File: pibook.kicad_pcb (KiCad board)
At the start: 2 copper layers, 85 x 85 mm, 122 parts, among them IC1 ATTINY48-A, J1 ComputeModule, J2 TRS_JACK_3PIN, P1 CONN_01X40, P2 USB_OTG, P3 CONN_01X02, P4 CONN_02X05, P5 USB_A, P6 CONN_02X06, P7 CONN_01X20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

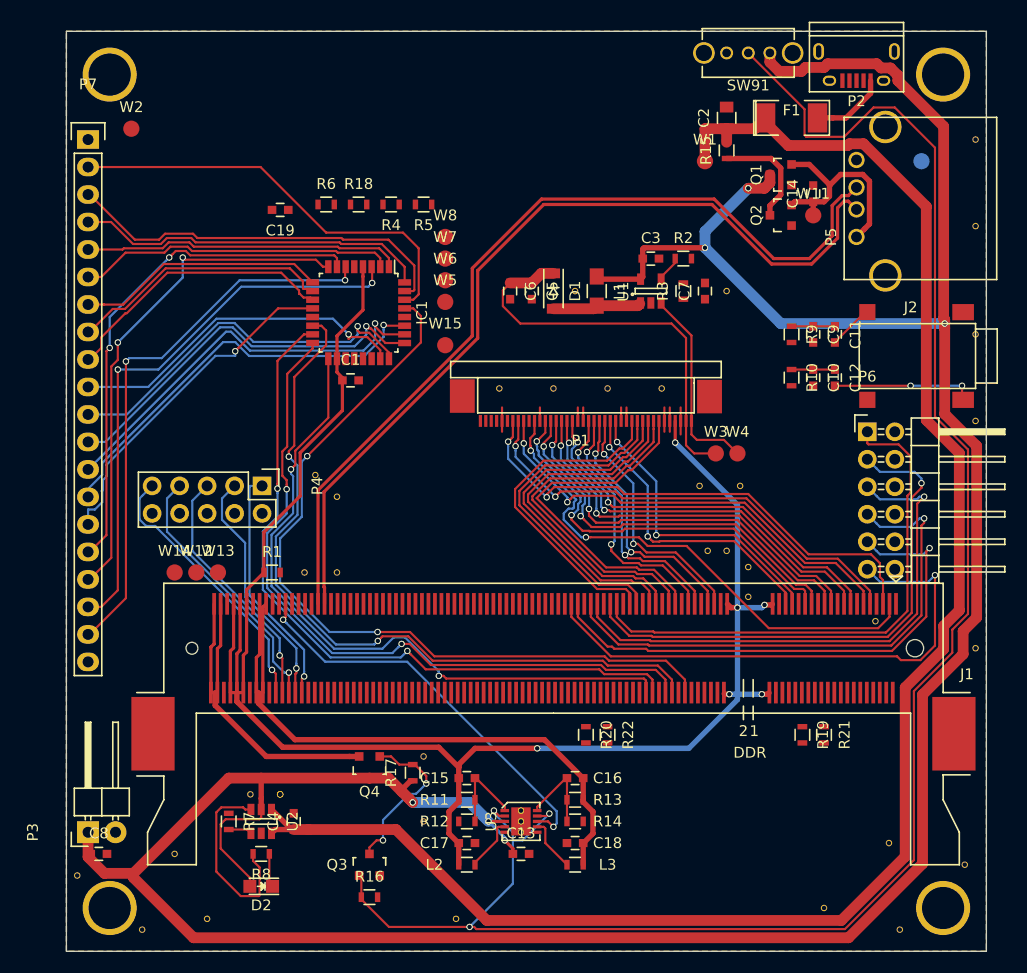
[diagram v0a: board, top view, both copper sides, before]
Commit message: Rounded corners!
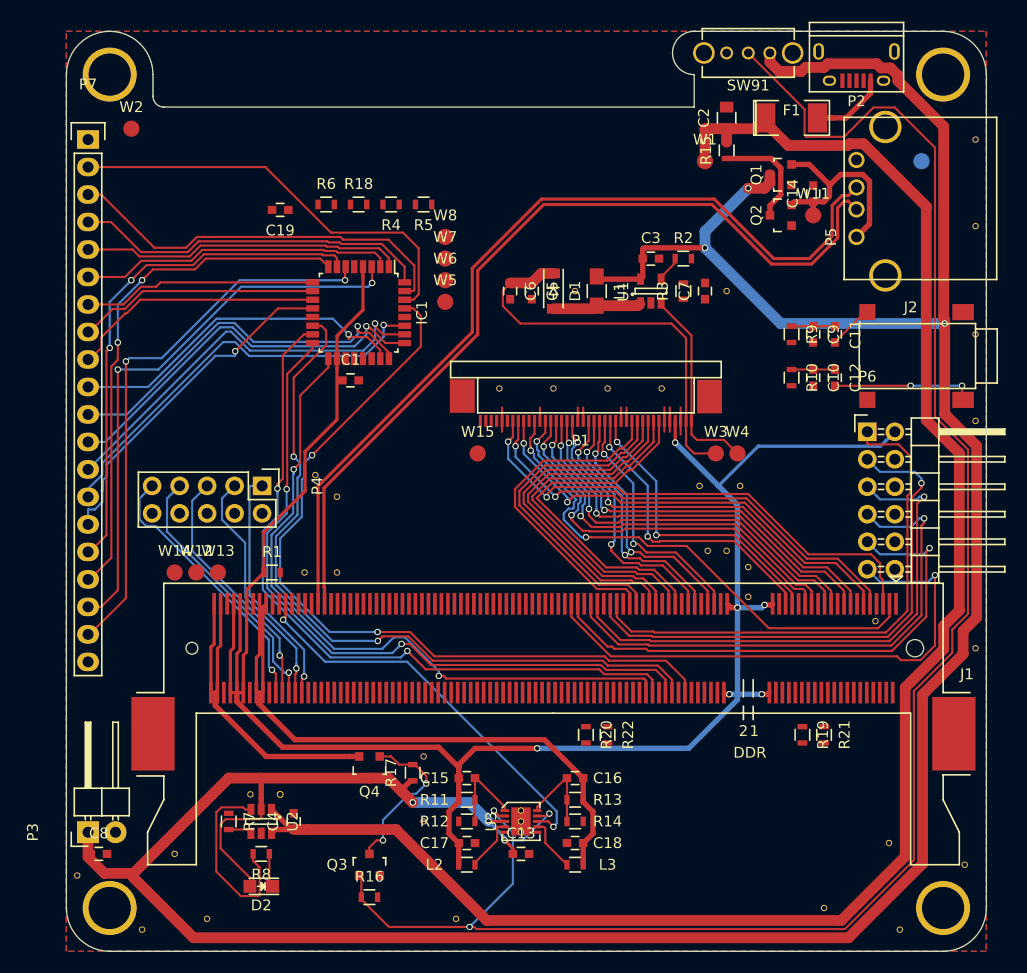
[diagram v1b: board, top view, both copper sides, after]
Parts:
- moved W15 10.4 mm to (111.0, 147.0)
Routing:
- net +3V3: track 161.1 -> 179.0 mm
- net /KEY_C7: track 25.8 -> 23.6 mm
- net /KEY_C6: track 24.4 -> 22.3 mm
- net /KEY_C5: track 23.0 -> 21.6 mm
- net /KEY_R3: track 47.3 -> 48.1 mm
- net /KEY_R2: track 47.2 -> 47.8 mm
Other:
- outline, holes or cut-outs redrawn

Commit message: 5V + some extra routing
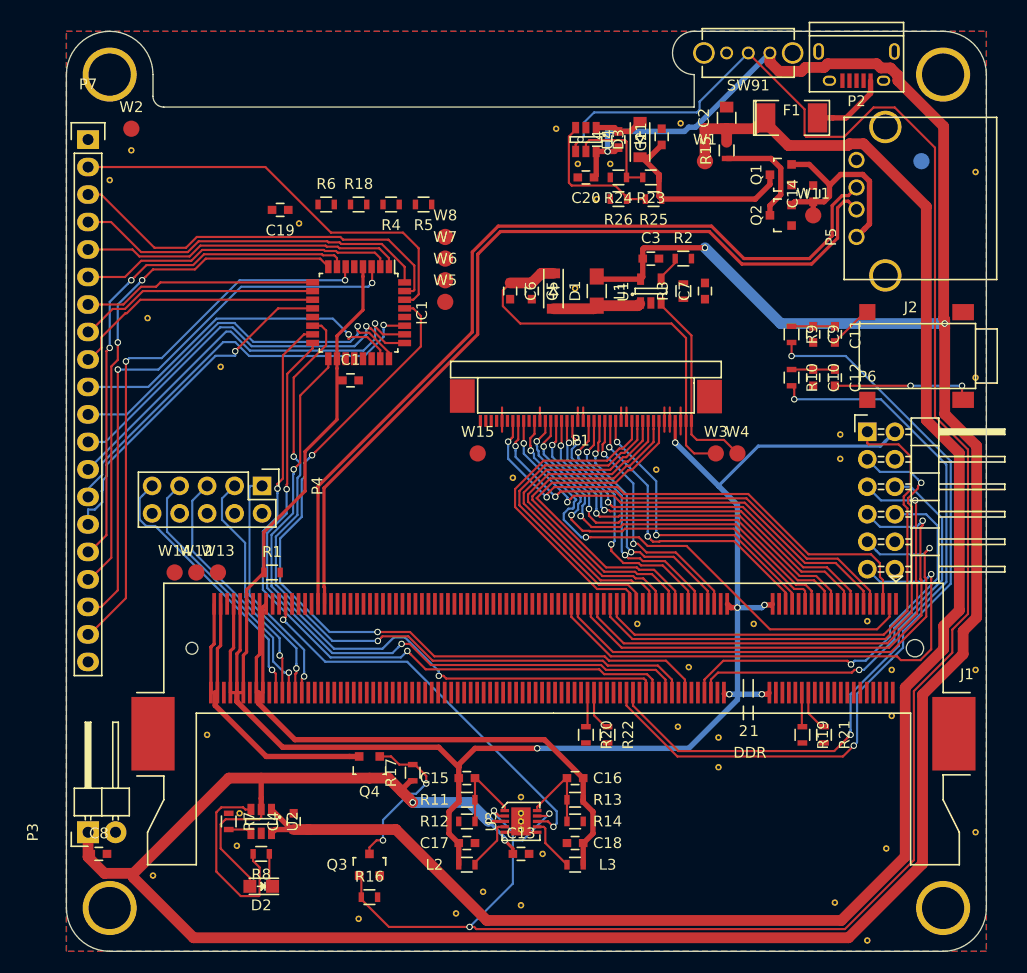
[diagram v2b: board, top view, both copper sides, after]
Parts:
- removed the REF** at (136.0, 157.5)
- removed the REF** at (120.0, 132.0)
- removed the REF** at (136.0, 160.2)
- removed the REF** at (132.2, 156.0)
- removed the REF** at (147.8, 162.5)
- removed the REF** at (96.0, 149.0)
- removed the REF** at (98.0, 151.0)
- removed the REF** at (98.0, 158.0)
- removed the REF** at (95.0, 158.0)
- removed the REF** at (157.0, 118.0)
- removed the REF** at (157.0, 126.0)
- removed the REF** at (134.0, 156.0)
- removed the REF** at (157.0, 136.0)
- removed the REF** at (157.0, 144.0)
- removed the REF** at (157.0, 165.0)
- removed the REF** at (149.0, 183.0)
- removed the REF** at (143.0, 189.0)
- removed the REF** at (86.0, 190.0)
- removed the REF** at (109.0, 190.0)
- removed the REF** at (74.0, 186.0)
- removed the REF** at (80.0, 191.0)
- removed the REF** at (83.0, 184.0)
- removed the REF** at (135.2, 150.0)
- removed the REF** at (90.0, 178.5)
- removed the REF** at (106.0, 181.0)
- removed the REF** at (92.8, 178.5) (x2)
- removed the REF** at (106.0, 175.0)
- removed the REF** at (115.0, 182.0)
- removed the REF** at (115.0, 180.0)
- removed the REF** at (150.0, 191.0)
- removed the REF** at (156.0, 185.0)
- removed the REF** at (131.5, 150.0)
- removed the REF** at (128.0, 141.0)
- removed the REF** at (123.0, 141.0)
- removed the REF** at (118.0, 141.0)
- removed the REF** at (113.0, 141.0)
- removed the REF** at (134.0, 132.0)
- added C20: 1u, Capacitors_SMD:C_0603, F.Cu at (121.0, 121.5)
- added C21: 1u, Capacitors_SMD:C_0603, F.Cu at (128.0, 117.8)
- added D3: MBR0540T3G, Diodes_SMD:SOD-123, F.Cu at (126.0, 118.0)
- added L4: 10u, Capacitors_SMD:C_0603, F.Cu at (124.0, 118.0)
- added R23: 47k, Resistors_SMD:R_0603, F.Cu at (127.0, 121.5)
- added R24: 10k, Resistors_SMD:R_0603, F.Cu at (124.0, 121.5)
- added R25: 40k, Resistors_SMD:R_0603, F.Cu at (127.2, 123.5)
- added R26: 10k, Resistors_SMD:R_0603, F.Cu at (124.0, 123.5)
- added REF**: VIA_0.6MM, ComputeModule:VIA_0.6MM, F.Cu at (144.0, 188.5)
- added REF**: VIA_0.6MM, ComputeModule:VIA_0.6MM, F.Cu at (117.0, 184.0)
- added REF**: VIA_0.6MM, ComputeModule:VIA_0.6MM, F.Cu at (115.0, 181.8)
- added REF**: VIA_0.6MM, ComputeModule:VIA_0.6MM, F.Cu at (115.0, 180.2)
- added REF**: VIA_0.6MM, ComputeModule:VIA_0.6MM, F.Cu at (120.0, 131.8)
- added REF**: VIA_0.6MM, ComputeModule:VIA_0.6MM, F.Cu at (79.0, 119.0)
- added REF**: VIA_0.6MM, ComputeModule:VIA_0.6MM, F.Cu at (94.5, 125.8)
- added REF**: VIA_0.6MM, ComputeModule:VIA_0.6MM, F.Cu at (77.0, 121.8)
- added REF**: VIA_0.6MM, ComputeModule:VIA_0.6MM, F.Cu at (80.5, 134.5)
- added REF**: VIA_0.6MM, ComputeModule:VIA_0.6MM, F.Cu at (87.2, 139.0)
- added REF**: VIA_0.6MM, ComputeModule:VIA_0.6MM, F.Cu at (148.8, 183.5)
- added REF**: VIA_0.6MM, ComputeModule:VIA_0.6MM, F.Cu at (149.2, 167.0)
- added REF**: VIA_0.6MM, ComputeModule:VIA_0.6MM, F.Cu at (130.5, 166.8)
- added REF**: VIA_0.6MM, ComputeModule:VIA_0.6MM, F.Cu at (133.2, 176.0)
- added REF**: VIA_0.6MM, ComputeModule:VIA_0.6MM, F.Cu at (129.5, 172.2)
- added REF**: VIA_0.6MM, ComputeModule:VIA_0.6MM, F.Cu at (115.0, 188.8)
- added REF**: VIA_0.6MM, ComputeModule:VIA_0.6MM, F.Cu at (111.5, 187.5)
- added REF**: VIA_0.6MM, ComputeModule:VIA_0.6MM, F.Cu at (109.0, 189.5)
- added REF**: VIA_0.6MM, ComputeModule:VIA_0.6MM, F.Cu at (88.8, 183.2)
- added REF**: VIA_0.6MM, ComputeModule:VIA_0.6MM, F.Cu at (89.0, 180.2)
- added REF**: VIA_0.6MM, ComputeModule:VIA_0.6MM, F.Cu at (86.0, 173.0)
- added REF**: VIA_0.6MM, ComputeModule:VIA_0.6MM, F.Cu at (149.2, 171.2)
- added REF**: VIA_0.6MM, ComputeModule:VIA_0.6MM, F.Cu at (100.0, 190.0)
- added REF**: VIA_0.6MM, ComputeModule:VIA_0.6MM, F.Cu at (81.0, 186.0)
- added REF**: VIA_0.6MM, ComputeModule:VIA_0.6MM, F.Cu at (157.0, 121.0)
- added REF**: VIA_0.6MM, ComputeModule:VIA_0.6MM, F.Cu at (157.0, 140.0)
- added REF**: VIA_0.6MM, ComputeModule:VIA_0.6MM, F.Cu at (157.0, 167.0)
- added REF**: VIA_0.6MM, ComputeModule:VIA_0.6MM, F.Cu at (157.0, 182.0)
- added REF**: VIA_0.6MM, ComputeModule:VIA_0.6MM, F.Cu at (147.0, 192.0)
- added REF**: VIA_0.6MM, ComputeModule:VIA_0.6MM, F.Cu at (147.0, 162.5)
- added REF**: VIA_0.6MM, ComputeModule:VIA_0.6MM, F.Cu at (136.5, 162.8)
- added REF**: VIA_0.6MM, ComputeModule:VIA_0.6MM, F.Cu at (125.8, 162.8)
- added REF**: VIA_0.6MM, ComputeModule:VIA_0.6MM, F.Cu at (133.2, 173.2)
- added REF**: VIA_0.6MM, ComputeModule:VIA_0.6MM, F.Cu at (129.8, 116.5)
- added REF**: VIA_0.6MM, ComputeModule:VIA_0.6MM, F.Cu at (118.2, 117.0)
- added REF**: VIA_0.6MM, ComputeModule:VIA_0.6MM, F.Cu at (122.0, 123.5)
- added REF**: VIA_0.6MM, ComputeModule:VIA_0.6MM, F.Cu at (123.2, 120.2)
- added REF**: VIA_0.6MM, ComputeModule:VIA_0.6MM, F.Cu at (120.2, 120.2)
- added REF**: VIA_0.6MM, ComputeModule:VIA_0.6MM, F.Cu at (114.2, 149.2)
- added REF**: VIA_0.6MM, ComputeModule:VIA_0.6MM, F.Cu at (127.5, 148.5)
- added REF**: VIA_0.6MM, ComputeModule:VIA_0.6MM, F.Cu at (144.5, 147.5)
- added REF**: VIA_0.6MM, ComputeModule:VIA_0.6MM, F.Cu at (144.5, 145.2)
- added REF**: VIA_0.6MM, ComputeModule:VIA_0.6MM, F.Cu at (115.0, 178.8)
- added U4: MIC2619YD6, TO_SOT_Packages_SMD:SOT-23-6, F.Cu at (121.0, 118.0)
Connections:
- Q1 pad 3: +BATT -> +5V
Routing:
- net /AUDIO_R_PWM: track 0.00 -> 74.5 mm, vias 0 -> 2
- net /AUDIO_L_PWM: track 0.00 -> 70.2 mm, vias 0 -> 2
- net /UART_TX: track 0.00 -> 38.3 mm, vias 0 -> 1
- net /UART_RX: track 0.00 -> 36.7 mm, vias 0 -> 1
- net /PWR_ENABLE: track 170.8 -> 192.0 mm, vias 3 -> 4
- net +5V: track 0.00 -> 18.7 mm
- net +BATT: track 284.8 -> 299.2 mm
- net Net-(R25-Pad2): track 0.00 -> 13.2 mm
- net Net-(R23-Pad2): track 0.00 -> 9.48 mm
- net Net-(D3-Pad2): track 0.00 -> 4.56 mm
- net Net-(J1-Pad28): track 0.00 -> 3.87 mm
- net Net-(J1-Pad82): track 0.00 -> 3.78 mm
- net Net-(J1-Pad84): track 0.00 -> 3.21 mm
- net GND: track 15.5 -> 18.7 mm
- net Net-(J1-Pad30): track 0.00 -> 3.17 mm
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
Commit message: All signals routed (still fails DRC)
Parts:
- added REF**: VIA_0.6MM, ComputeModule:VIA_0.6MM, F.Cu at (152.5, 148.0)
- added REF**: VIA_0.6MM, ComputeModule:VIA_0.6MM, F.Cu at (80.0, 158.8)
- added REF**: VIA_0.6MM, ComputeModule:VIA_0.6MM, F.Cu at (83.2, 164.0)
- added REF**: VIA_0.6MM, ComputeModule:VIA_0.6MM, F.Cu at (83.5, 147.8)
- added REF**: VIA_0.6MM, ComputeModule:VIA_0.6MM, F.Cu at (93.8, 171.0)
- added REF**: VIA_0.6MM, ComputeModule:VIA_0.6MM, F.Cu at (125.0, 172.8)
- added REF**: VIA_0.6MM, ComputeModule:VIA_0.6MM, F.Cu at (99.2, 142.0)
- added REF**: VIA_0.6MM, ComputeModule:VIA_0.6MM, F.Cu at (99.0, 137.0)
- added REF**: VIA_0.6MM, ComputeModule:VIA_0.6MM, F.Cu at (98.2, 133.0)
- moved R18 28.2 mm to (111.0, 150.0)
- moved W8 24.8 mm to (91.0, 145.0), turned to 90 degrees
- moved C19 23.5 mm to (116.0, 121.0), turned to 0 degrees
- moved W7 22.0 mm to (91.0, 143.0), turned to 90 degrees
- moved W6 19.7 mm to (91.0, 141.0), turned to 90 degrees
- moved W5 18.0 mm to (91.0, 139.0), turned to 90 degrees
- moved R4 14.8 mm to (116.0, 117.0)
- moved R6 12.2 mm to (107.0, 131.0), turned to 270 degrees
- moved R5 11.2 mm to (116.0, 119.0), turned to 0 degrees
- moved W13 7.28 mm to (94.0, 156.0)
- moved W12 4.12 mm to (89.0, 157.0)
- moved W14 3.16 mm to (86.0, 157.0)
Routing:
- net /ANALOG1: track 0.00 -> 133.3 mm, vias 0 -> 1
- net /ANALOG0: track 0.00 -> 132.2 mm, vias 0 -> 1
- net /BACKL_PWM: track 2.44 -> 120.0 mm, vias 0 -> 2
- net /LCD_DISP_ON: track 0.00 -> 73.7 mm, vias 0 -> 2
- net +3V3: track 179.0 -> 227.7 mm, vias 6 -> 8
- net Net-(C19-Pad1): track 0.00 -> 27.2 mm, vias 0 -> 2
- net /AVR_~RST: track 74.1 -> 84.5 mm, vias 2 -> 3
- net +1V8: track 59.9 -> 68.8 mm
- net +BATT: track 299.2 -> 306.4 mm, vias 6 -> 7
- net Net-(C12-Pad2): track 13.1 -> 19.9 mm
- net /AVR_SCK: track 63.6 -> 69.1 mm, vias 2 -> 4
- net /AVR_MISO: track 66.6 -> 71.1 mm, vias 2 -> 4
- net /CM_VBAT: track 33.7 -> 37.9 mm
- net GND: track 18.7 -> 22.2 mm
- net /AVR_MOSI: track 67.1 -> 70.5 mm
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
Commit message: Corrected some DRC
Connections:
- J1 pad 10: (no net) -> Net-(J1-Pad10)
- J1 pad 100: (no net) -> Net-(J1-Pad100)
- J1 pad 101: (no net) -> Net-(J1-Pad101)
- J1 pad 102: (no net) -> Net-(J1-Pad102)
- J1 pad 105: (no net) -> Net-(J1-Pad105)
- J1 pad 106: (no net) -> Net-(J1-Pad106)
- J1 pad 107: (no net) -> Net-(J1-Pad107)
- J1 pad 108: (no net) -> Net-(J1-Pad108)
- J1 pad 111: (no net) -> Net-(J1-Pad111)
- J1 pad 112: (no net) -> Net-(J1-Pad112)
- J1 pad 113: (no net) -> Net-(J1-Pad113)
- J1 pad 114: (no net) -> Net-(J1-Pad114)
- J1 pad 117: (no net) -> Net-(J1-Pad117)
- J1 pad 118: (no net) -> Net-(J1-Pad118)
- J1 pad 119: (no net) -> Net-(J1-Pad119)
- J1 pad 12: (no net) -> Net-(J1-Pad12)
- J1 pad 120: (no net) -> Net-(J1-Pad120)
- J1 pad 123: (no net) -> Net-(J1-Pad123)
- J1 pad 124: (no net) -> Net-(J1-Pad124)
- J1 pad 125: (no net) -> Net-(J1-Pad125)
- J1 pad 126: (no net) -> Net-(J1-Pad126)
- J1 pad 128: (no net) -> Net-(J1-Pad128)
- J1 pad 129: (no net) -> Net-(J1-Pad129)
- J1 pad 130: (no net) -> Net-(J1-Pad130)
- J1 pad 131: (no net) -> Net-(J1-Pad131)
- J1 pad 132: (no net) -> Net-(J1-Pad132)
- J1 pad 135: (no net) -> Net-(J1-Pad135)
- J1 pad 136: (no net) -> Net-(J1-Pad136)
- J1 pad 137: (no net) -> Net-(J1-Pad137)
- J1 pad 138: (no net) -> Net-(J1-Pad138)
- J1 pad 14: (no net) -> Net-(J1-Pad14)
- J1 pad 141: (no net) -> Net-(J1-Pad141)
- J1 pad 142: (no net) -> Net-(J1-Pad142)
- J1 pad 143: (no net) -> Net-(J1-Pad143)
- J1 pad 144: (no net) -> Net-(J1-Pad144)
- J1 pad 147: (no net) -> Net-(J1-Pad147)
- J1 pad 148: (no net) -> Net-(J1-Pad148)
- J1 pad 149: (no net) -> Net-(J1-Pad149)
- J1 pad 150: (no net) -> Net-(J1-Pad150)
- J1 pad 153: (no net) -> Net-(J1-Pad153)
- J1 pad 154: (no net) -> Net-(J1-Pad154)
- J1 pad 155: (no net) -> Net-(J1-Pad155)
- J1 pad 156: (no net) -> Net-(J1-Pad156)
- J1 pad 158: (no net) -> Net-(J1-Pad158)
- J1 pad 159: (no net) -> Net-(J1-Pad159)
- J1 pad 16: (no net) -> Net-(J1-Pad16)
- J1 pad 160: (no net) -> Net-(J1-Pad160)
- J1 pad 161: (no net) -> Net-(J1-Pad161)
- J1 pad 162: (no net) -> Net-(J1-Pad162)
- J1 pad 166: (no net) -> Net-(J1-Pad166)
- J1 pad 171: (no net) -> Net-(J1-Pad171)
- J1 pad 173: (no net) -> Net-(J1-Pad173)
- J1 pad 175: (no net) -> Net-(J1-Pad175)
- J1 pad 179: (no net) -> Net-(J1-Pad179)
- J1 pad 18: (no net) -> Net-(J1-Pad18)
- J1 pad 20: (no net) -> Net-(J1-Pad20)
- J1 pad 22: (no net) -> Net-(J1-Pad22)
- J1 pad 24: (no net) -> Net-(J1-Pad24)
- J1 pad 34: (no net) -> Net-(J1-Pad34)
- J1 pad 36: (no net) -> Net-(J1-Pad36)
- J1 pad 4: (no net) -> Net-(J1-Pad4)
- J1 pad 52: (no net) -> Net-(J1-Pad52)
- J1 pad 6: (no net) -> Net-(J1-Pad6)
- J1 pad 76: (no net) -> Net-(J1-Pad76)
- J1 pad 78: (no net) -> Net-(J1-Pad78)
- J1 pad 8: (no net) -> Net-(J1-Pad8)
- J1 pad 88: (no net) -> Net-(J1-Pad88)
- J1 pad 90: (no net) -> Net-(J1-Pad90)
- J1 pad 93: (no net) -> Net-(J1-Pad93)
- J1 pad 94: (no net) -> Net-(J1-Pad94)
- J1 pad 95: (no net) -> Net-(J1-Pad95)
- J1 pad 96: (no net) -> Net-(J1-Pad96)
- J1 pad 99: (no net) -> Net-(J1-Pad99)
- P1 pad 35: (no net) -> Net-(P1-Pad35)
- P1 pad 37: (no net) -> Net-(P1-Pad37)
- P1 pad 38: (no net) -> Net-(P1-Pad38)
- P1 pad 39: (no net) -> Net-(P1-Pad39)
- P1 pad 40: (no net) -> Net-(P1-Pad40)
- P2 pad 2: (no net) -> Net-(P2-Pad2)
- P2 pad 3: (no net) -> Net-(P2-Pad3)
- P2 pad 4: (no net) -> Net-(P2-Pad4)
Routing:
- net /LCD_B_7: track 40.3 -> 37.2 mm
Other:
- net class Default: clearance 0.2 -> 0.199
- rule pad_to_mask_clearance: 0 -> 0.01
- rule trace_clearance: 0.2 -> 0.199

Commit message: Working on new switchmode layout
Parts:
- added TP1: Tie_point, ComputeModule:tiepoint-0.3, F.Cu at (114.5, 182.5)
- moved R14 11.3 mm to (131.0, 183.5)
- moved R13 8.06 mm to (127.0, 183.0)
- moved C15 7.83 mm to (106.5, 184.0)
- moved C16 6.96 mm to (126.5, 179.5)
- moved C18 6.52 mm to (116.5, 177.5)
- moved C13 6.02 mm to (110.5, 180.0), turned to 90 degrees
- moved C17 5.52 mm to (109.5, 177.5)
- moved L3 5.34 mm to (119.0, 179.8), turned to 90 degrees
- moved L2 5.22 mm to (108.5, 180.0), turned to 90 degrees
- moved R12 5.06 mm to (109.2, 186.0)
- moved R11 4.92 mm to (105.5, 181.0)
- moved REF** 4.78 mm to (111.5, 175.5)
- moved REF** 4.37 mm to (104.8, 188.5)
- moved R17 1.25 mm to (104.0, 175.8)
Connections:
- C13 pad 2: GND -> GNDPWR
- C17 pad 2: GND -> GNDPWR
- C18 pad 2: GND -> GNDPWR
- J1 pad 10: Net-(J1-Pad10) -> (no net)
- J1 pad 100: Net-(J1-Pad100) -> (no net)
- J1 pad 101: Net-(J1-Pad101) -> (no net)
- J1 pad 102: Net-(J1-Pad102) -> (no net)
- J1 pad 105: Net-(J1-Pad105) -> (no net)
- J1 pad 106: Net-(J1-Pad106) -> (no net)
- J1 pad 107: Net-(J1-Pad107) -> (no net)
- J1 pad 108: Net-(J1-Pad108) -> (no net)
- J1 pad 111: Net-(J1-Pad111) -> (no net)
- J1 pad 112: Net-(J1-Pad112) -> (no net)
- J1 pad 113: Net-(J1-Pad113) -> (no net)
- J1 pad 114: Net-(J1-Pad114) -> (no net)
- J1 pad 117: Net-(J1-Pad117) -> (no net)
- J1 pad 118: Net-(J1-Pad118) -> (no net)
- J1 pad 119: Net-(J1-Pad119) -> (no net)
- J1 pad 12: Net-(J1-Pad12) -> (no net)
- J1 pad 120: Net-(J1-Pad120) -> (no net)
- J1 pad 123: Net-(J1-Pad123) -> (no net)
- J1 pad 124: Net-(J1-Pad124) -> (no net)
- J1 pad 125: Net-(J1-Pad125) -> (no net)
- J1 pad 126: Net-(J1-Pad126) -> (no net)
- J1 pad 128: Net-(J1-Pad128) -> (no net)
- J1 pad 129: Net-(J1-Pad129) -> (no net)
- J1 pad 130: Net-(J1-Pad130) -> (no net)
- J1 pad 131: Net-(J1-Pad131) -> (no net)
- J1 pad 132: Net-(J1-Pad132) -> (no net)
- J1 pad 135: Net-(J1-Pad135) -> (no net)
- J1 pad 136: Net-(J1-Pad136) -> (no net)
- J1 pad 137: Net-(J1-Pad137) -> (no net)
- J1 pad 138: Net-(J1-Pad138) -> (no net)
- J1 pad 14: Net-(J1-Pad14) -> (no net)
- J1 pad 141: Net-(J1-Pad141) -> (no net)
- J1 pad 142: Net-(J1-Pad142) -> (no net)
- J1 pad 143: Net-(J1-Pad143) -> (no net)
- J1 pad 144: Net-(J1-Pad144) -> (no net)
- J1 pad 147: Net-(J1-Pad147) -> (no net)
- J1 pad 148: Net-(J1-Pad148) -> (no net)
- J1 pad 149: Net-(J1-Pad149) -> (no net)
- J1 pad 150: Net-(J1-Pad150) -> (no net)
- J1 pad 153: Net-(J1-Pad153) -> (no net)
- J1 pad 154: Net-(J1-Pad154) -> (no net)
- J1 pad 155: Net-(J1-Pad155) -> (no net)
- J1 pad 156: Net-(J1-Pad156) -> (no net)
- J1 pad 158: Net-(J1-Pad158) -> (no net)
- J1 pad 159: Net-(J1-Pad159) -> (no net)
- J1 pad 16: Net-(J1-Pad16) -> (no net)
- J1 pad 160: Net-(J1-Pad160) -> (no net)
- J1 pad 161: Net-(J1-Pad161) -> (no net)
- J1 pad 162: Net-(J1-Pad162) -> (no net)
- J1 pad 166: Net-(J1-Pad166) -> (no net)
- J1 pad 171: Net-(J1-Pad171) -> (no net)
- J1 pad 173: Net-(J1-Pad173) -> (no net)
- J1 pad 175: Net-(J1-Pad175) -> (no net)
- J1 pad 179: Net-(J1-Pad179) -> (no net)
- J1 pad 18: Net-(J1-Pad18) -> (no net)
- J1 pad 20: Net-(J1-Pad20) -> (no net)
- J1 pad 22: Net-(J1-Pad22) -> (no net)
- J1 pad 24: Net-(J1-Pad24) -> (no net)
- J1 pad 34: Net-(J1-Pad34) -> (no net)
- J1 pad 36: Net-(J1-Pad36) -> (no net)
- J1 pad 4: Net-(J1-Pad4) -> (no net)
- J1 pad 52: Net-(J1-Pad52) -> (no net)
- J1 pad 6: Net-(J1-Pad6) -> (no net)
- J1 pad 76: Net-(J1-Pad76) -> (no net)
- J1 pad 78: Net-(J1-Pad78) -> (no net)
- J1 pad 8: Net-(J1-Pad8) -> (no net)
- J1 pad 88: Net-(J1-Pad88) -> (no net)
- J1 pad 90: Net-(J1-Pad90) -> (no net)
- J1 pad 93: Net-(J1-Pad93) -> (no net)
- J1 pad 94: Net-(J1-Pad94) -> (no net)
- J1 pad 95: Net-(J1-Pad95) -> (no net)
- J1 pad 96: Net-(J1-Pad96) -> (no net)
- J1 pad 99: Net-(J1-Pad99) -> (no net)
- P1 pad 35: Net-(P1-Pad35) -> (no net)
- P1 pad 37: Net-(P1-Pad37) -> (no net)
- P1 pad 38: Net-(P1-Pad38) -> (no net)
- P1 pad 39: Net-(P1-Pad39) -> (no net)
- P1 pad 40: Net-(P1-Pad40) -> (no net)
- P2 pad 2: Net-(P2-Pad2) -> (no net)
- P2 pad 3: Net-(P2-Pad3) -> (no net)
- P2 pad 4: Net-(P2-Pad4) -> (no net)
- R16 pad 2: GND -> GNDPWR
- REF** pad 1: GND -> GNDPWR (x3)
- U3 pad 5: GND -> GNDPWR
- U3 pad 6: GND -> GNDPWR
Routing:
- net +1V8: track 68.8 -> 59.5 mm
- net +3V3: track 227.7 -> 218.4 mm
- net Net-(C16-Pad2): track 8.20 -> 0.00 mm
- net Net-(C15-Pad2): track 8.20 -> 0.00 mm
- net GNDPWR: track 0.00 -> 3.21 mm
- net +BATT: track 306.4 -> 304.2 mm, vias 7 -> 6
- net Net-(Q3-Pad3): track 15.1 -> 13.5 mm
- net /PWR_ENABLE: track 192.0 -> 193.6 mm
- net Net-(L2-Pad1): track 4.99 -> 6.40 mm
- net GND: track 22.2 -> 21.0 mm
- net +VUSB_IN: track 159.7 -> 160.5 mm
- added copper zone on F.Cu, net GNDPWR
